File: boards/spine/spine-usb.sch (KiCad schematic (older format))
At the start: 34 parts, among them P1 USB_B, U1 93C56, U2 FT2232H, Y1 12 MHz

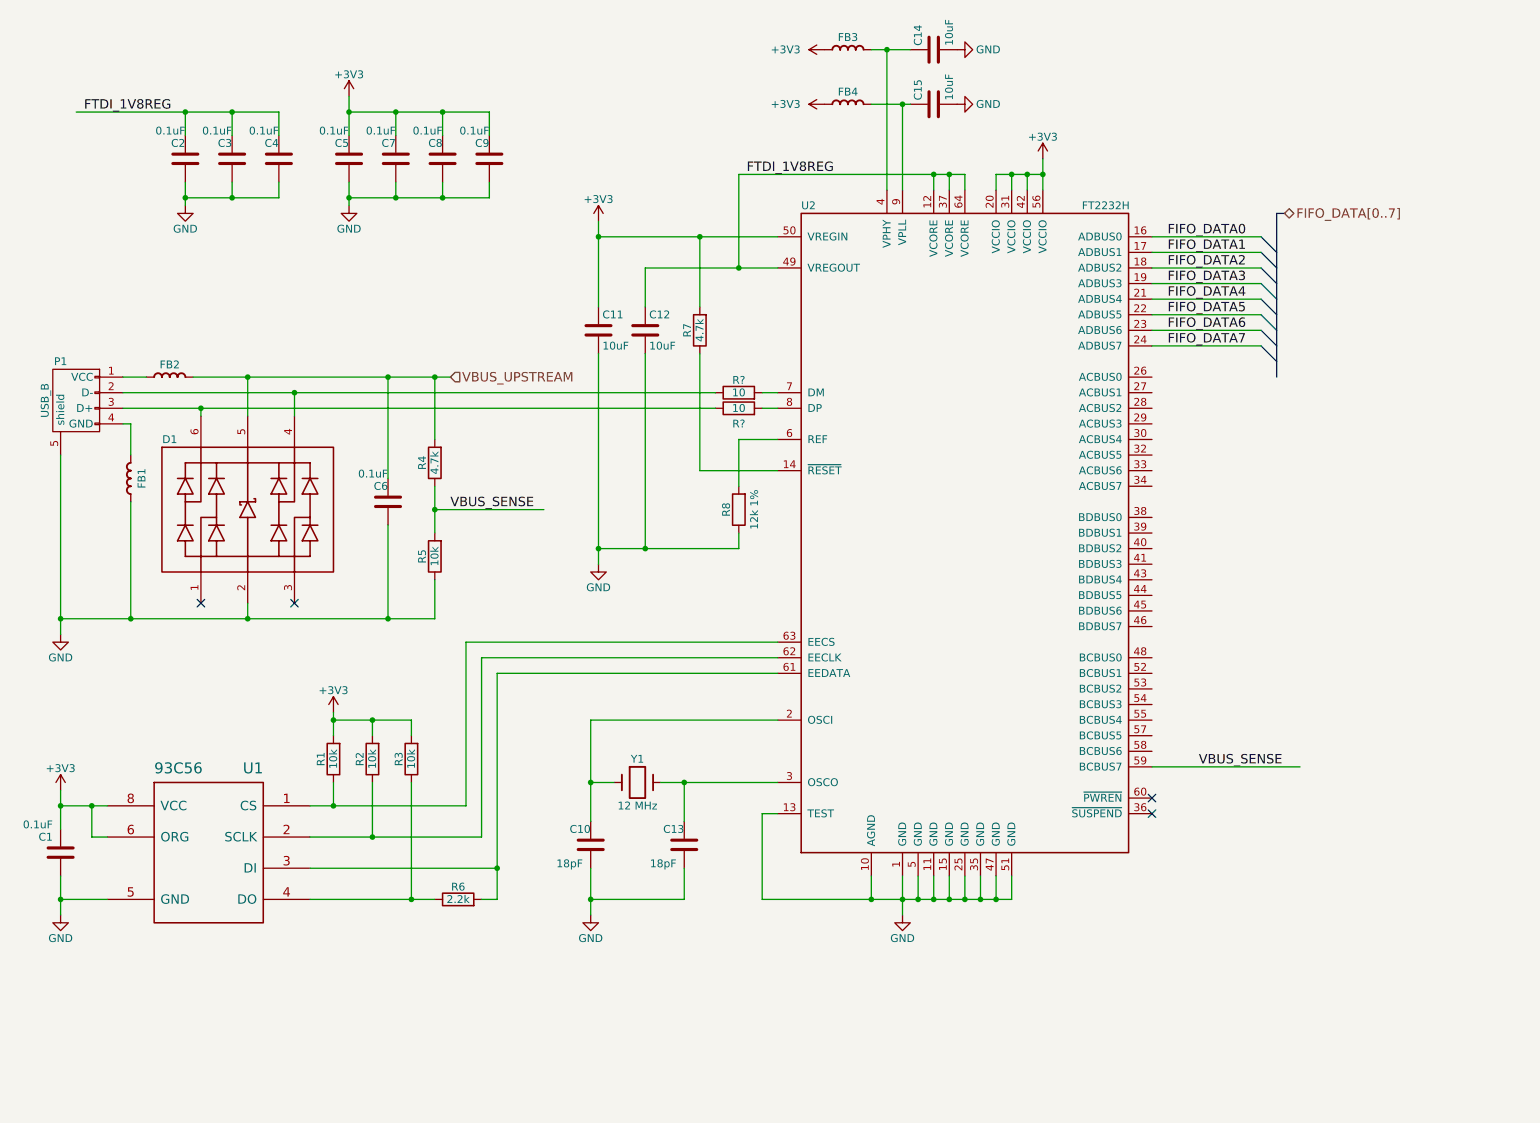
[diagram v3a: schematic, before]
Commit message: More schematic work: module ports and USB
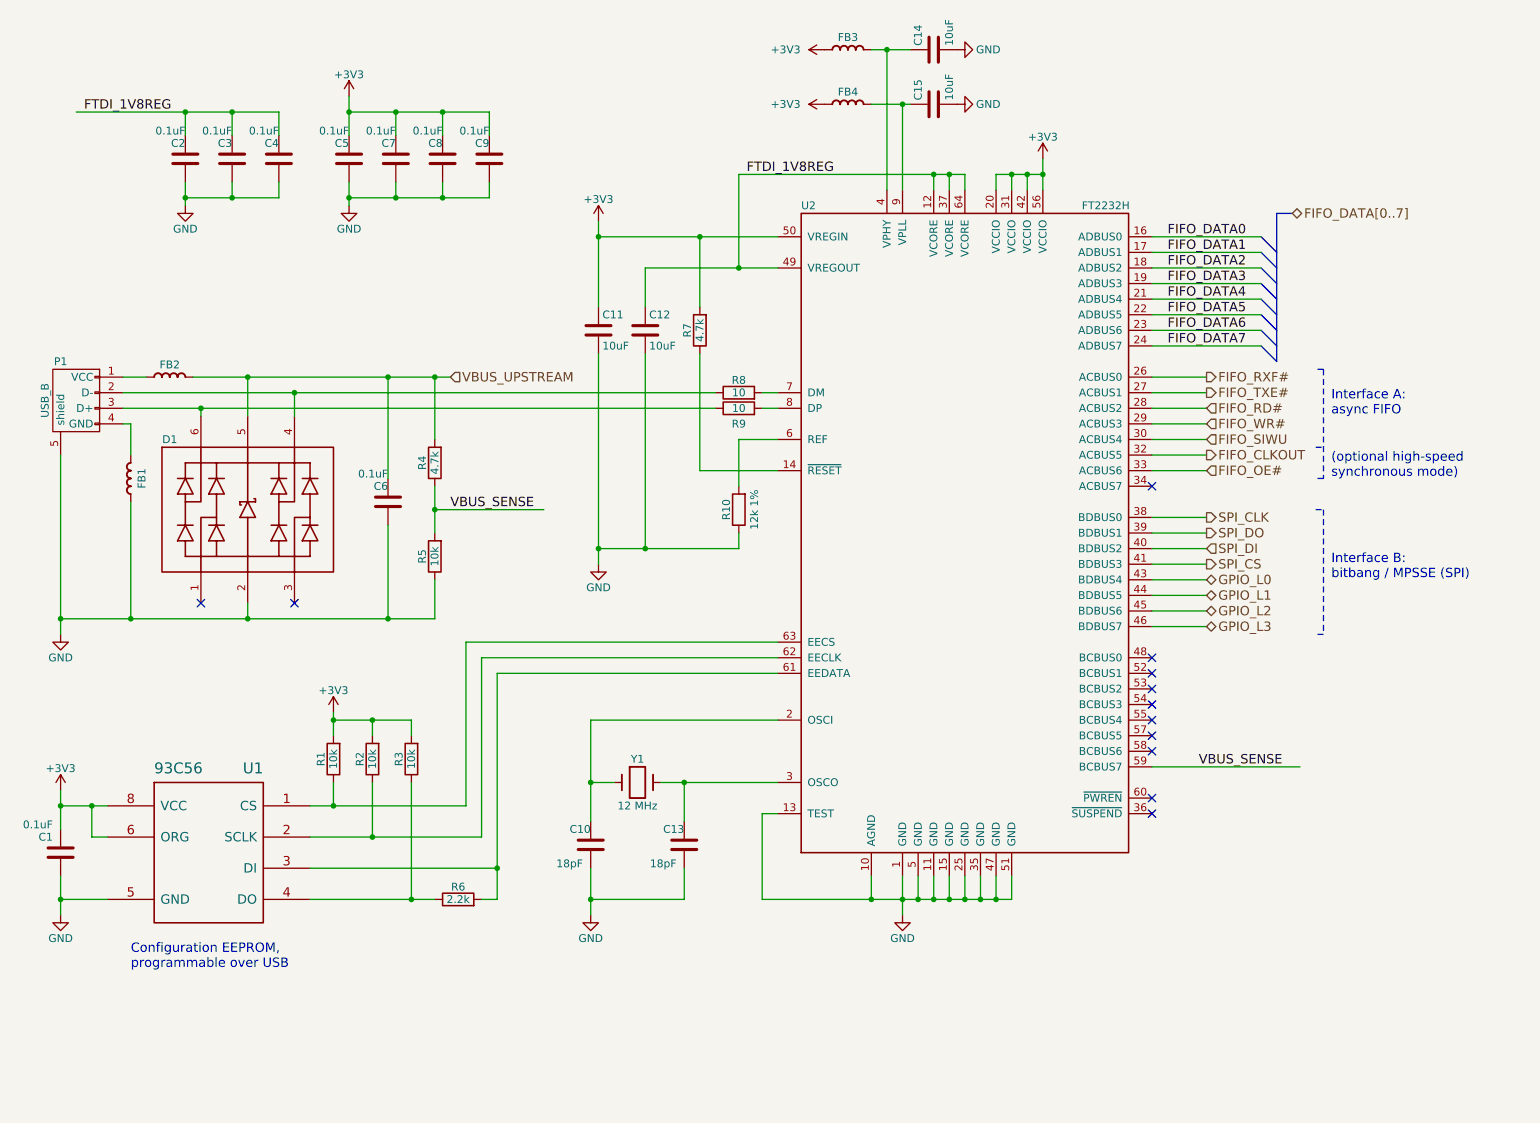
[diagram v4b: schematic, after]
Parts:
- gave numbers to parts that had none: 2
- renumbered R8 to R10
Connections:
- net labels added: FIFO_CLKOUT, FIFO_OE#, FIFO_RD#, FIFO_RXF#, FIFO_SIWU, FIFO_TXE#, FIFO_WR#, GPIO_L0, GPIO_L1, GPIO_L2, GPIO_L3, SPI_CLK, SPI_CS, SPI_DI, SPI_DO
- wire segments 119 -> 134
- no-connect marks 4 -> 12
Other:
- note added: "(optional high-speed\nsynchronous mode)"
- note added: "Configuration EEPROM,\nprogrammable over USB"
- note added: "Interface A:\nasync FIFO"
- note added: "Interface B:\nbitbang / MPSSE (SPI)"
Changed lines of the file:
@@
 $Descr USLetter 11000 8500
 encoding utf-8
-Sheet 2 4
+Sheet 2 5
 Title ""
 Date ""
@@
 	0    -1   1    0
 $EndComp
-Text HLabel 8900 1900 2    60   BiDi ~ 0
+Text HLabel 8950 1900 2    60   BiDi ~ 0
 FIFO_DATA[0..7]
 Entry Bus Bus
@@
 VBUS_SENSE
 $Comp
-L R R8
+L R R10
 U 1 1 563F3115
 P 5400 3800
-F 0 "R8" V 5480 3800 50  0000 C CNN
+F 0 "R10" V 5480 3800 50  0000 C CNN
 F 1 "12k 1%" V 5300 3800 50  0000 C CNN
 F 2 "" V 5330 3800 30  0000 C CNN
@@
 $EndComp
 $Comp
-L GND #PWR1
+L GND #PWR01
 U 1 1 563F3C00
 P 1050 4600
-F 0 "#PWR1" H 1050 4350 50  0001 C CNN
+F 0 "#PWR01" H 1050 4350 50  0001 C CNN
 F 1 "GND" H 1050 4450 50  0000 C CNN
 F 2 "" H 1050 4600 60  0000 C CNN
@@
 $EndComp
 $Comp
-L +3V3 #PWR9
+L +3V3 #PWR02
 U 1 1 563F5B33
 P 4500 1950
-F 0 "#PWR9" H 4500 1800 50  0001 C CNN
+F 0 "#PWR02" H 4500 1800 50  0001 C CNN
 F 1 "+3V3" H 4500 2090 50  0000 C CNN
 F 2 "" H 4500 1950 60  0000 C CNN
@@
 $EndComp
 $Comp
-L GND #PWR10
+L GND #PWR03
 U 1 1 56407FC9
 P 4500 4150
-F 0 "#PWR10" H 4500 3900 50  0001 C CNN
+F 0 "#PWR03" H 4500 3900 50  0001 C CNN
 F 1 "GND" H 4500 4000 50  0000 C CNN
 F 2 "" H 4500 4150 60  0000 C CNN
@@
 $EndComp
 $Comp
-L +3V3 #PWR12
+L +3V3 #PWR04
 U 1 1 56409317
 P 5950 1200
-F 0 "#PWR12" H 5950 1050 50  0001 C CNN
+F 0 "#PWR04" H 5950 1050 50  0001 C CNN
 F 1 "+3V3" V 5950 1450 50  0000 C CNN
 F 2 "" H 5950 1200 60  0000 C CNN
@@
 $EndComp
 $Comp
-L GND #PWR15
+L GND #PWR05
 U 1 1 56409352
 P 6800 1200
-F 0 "#PWR15" H 6800 950 50  0001 C CNN
+F 0 "#PWR05" H 6800 950 50  0001 C CNN
 F 1 "GND" V 6800 1000 50  0000 C CNN
 F 2 "" H 6800 1200 60  0000 C CNN
@@
 $EndComp
 $Comp
-L +3V3 #PWR11
+L +3V3 #PWR06
 U 1 1 564099D6
 P 5950 850
-F 0 "#PWR11" H 5950 700 50  0001 C CNN
+F 0 "#PWR06" H 5950 700 50  0001 C CNN
 F 1 "+3V3" V 5950 1100 50  0000 C CNN
 F 2 "" H 5950 850 60  0000 C CNN
@@
 $EndComp
 $Comp
-L GND #PWR14
+L GND #PWR07
 U 1 1 564099DC
 P 6800 850
-F 0 "#PWR14" H 6800 600 50  0001 C CNN
+F 0 "#PWR07" H 6800 600 50  0001 C CNN
 F 1 "GND" V 6800 650 50  0000 C CNN
 F 2 "" H 6800 850 60  0000 C CNN
@@
 $EndComp
 $Comp
-L +3V3 #PWR16
+L +3V3 #PWR08
 U 1 1 56409B2C
 P 7350 1550
-F 0 "#PWR16" H 7350 1400 50  0001 C CNN
+F 0 "#PWR08" H 7350 1400 50  0001 C CNN
 F 1 "+3V3" H 7350 1690 50  0000 C CNN
 F 2 "" H 7350 1550 60  0000 C CNN
@@
 $EndComp
 $Comp
-L +3V3 #PWR2
+L +3V3 #PWR09
 U 1 1 5640C498
 P 1050 5600
-F 0 "#PWR2" H 1050 5450 50  0001 C CNN
+F 0 "#PWR09" H 1050 5450 50  0001 C CNN
 F 1 "+3V3" H 1050 5740 50  0000 C CNN
 F 2 "" H 1050 5600 60  0000 C CNN
@@
 $EndComp
 $Comp
-L GND #PWR3
+L GND #PWR010
 U 1 1 5640C700
 P 1050 6400
-F 0 "#PWR3" H 1050 6150 50  0001 C CNN
+F 0 "#PWR010" H 1050 6150 50  0001 C CNN
 F 1 "GND" H 1050 6250 50  0000 C CNN
 F 2 "" H 1050 6400 60  0000 C CNN
@@
 $EndComp
 $Comp
-L +3V3 #PWR5
+L +3V3 #PWR011
 U 1 1 5640CB0D
 P 2800 5100
-F 0 "#PWR5" H 2800 4950 50  0001 C CNN
+F 0 "#PWR011" H 2800 4950 50  0001 C CNN
 F 1 "+3V3" H 2800 5240 50  0000 C CNN
 F 2 "" H 2800 5100 60  0000 C CNN
@@
 $EndComp
 $Comp
-L GND #PWR4
+L GND #PWR012
 U 1 1 5640EC58
 P 1850 1850
-F 0 "#PWR4" H 1850 1600 50  0001 C CNN
+F 0 "#PWR012" H 1850 1600 50  0001 C CNN
 F 1 "GND" H 1850 1700 50  0000 C CNN
 F 2 "" H 1850 1850 60  0000 C CNN
@@
 $EndComp
 $Comp
-L GND #PWR7
+L GND #PWR013
 U 1 1 5640ECEA
 P 2900 1850
-F 0 "#PWR7" H 2900 1600 50  0001 C CNN
+F 0 "#PWR013" H 2900 1600 50  0001 C CNN
 F 1 "GND" H 2900 1700 50  0000 C CNN
 F 2 "" H 2900 1850 60  0000 C CNN
@@
 FTDI_1V8REG
 $Comp
-L +3V3 #PWR6
+L +3V3 #PWR014
 U 1 1 5640F443
 P 2900 1150
-F 0 "#PWR6" H 2900 1000 50  0001 C CNN
+F 0 "#PWR014" H 2900 1000 50  0001 C CNN
 F 1 "+3V3" H 2900 1290 50  0000 C CNN
 F 2 "" H 2900 1150 60  0000 C CNN
@@
 $EndComp
 $Comp
-L GND #PWR8
+L GND #PWR015
 U 1 1 56411C34
 P 4450 6400
-F 0 "#PWR8" H 4450 6150 50  0001 C CNN
+F 0 "#PWR015" H 4450 6150 50  0001 C CNN
 F 1 "GND" H 4450 6250 50  0000 C CNN
 F 2 "" H 4450 6400 60  0000 C CNN
@@
 $EndComp
 $Comp
-L GND #PWR13
+L GND #PWR016
 U 1 1 56412014
 P 6450 6400
-F 0 "#PWR13" H 6450 6150 50  0001 C CNN
+F 0 "#PWR016" H 6450 6150 50  0001 C CNN
 F 1 "GND" H 6450 6250 50  0000 C CNN
 F 2 "" H 6450 6400 60  0000 C CNN
@@
 	8050 2050 8750 2050
 Wire Bus Line
-	8850 1900 8850 2950
+	8850 1900 8850 2850
 Wire Bus Line
-	8850 1900 8900 1900
+	8850 1900 8950 1900
 Wire Wire Line
 	1450 2950 1600 2950
@@
 Connection ~ 4450 6300
 $Comp
-L R R?
+L R R8
 U 1 1 56413618
 P 5400 3050
-F 0 "R?" V 5480 3050 50  0000 C CNN
+F 0 "R8" V 5480 3050 50  0000 C CNN
 F 1 "10" V 5400 3050 50  0000 C CNN
 F 2 "" V 5330 3050 30  0000 C CNN
@@
 $EndComp
 $Comp
-L R R?
+L R R9
 U 1 1 56413B05
 P 5400 3150
-F 0 "R?" V 5300 3150 50  0000 C CNN
+F 0 "R9" V 5300 3150 50  0000 C CNN
 F 1 "10" V 5400 3150 50  0000 C CNN
 F 2 "" V 5330 3150 30  0000 C CNN
@@
 Wire Wire Line
 	5650 3150 5550 3150
+Text HLabel 8400 2950 2    60   Output ~ 0
+FIFO_RXF#
+Text HLabel 8400 3050 2    60   Output ~ 0
+FIFO_TXE#
+Text HLabel 8400 3150 2    60   Input ~ 0
+FIFO_RD#
+Text HLabel 8400 3250 2    60   Input ~ 0
+FIFO_WR#
+Text HLabel 8400 3350 2    60   Input ~ 0
+FIFO_SIWU
+Text HLabel 8400 3450 2    60   Output ~ 0
+FIFO_CLKOUT
+Text HLabel 8400 3550 2    60   Input ~ 0
+FIFO_OE#
+Wire Notes Line
+	9100 3400 9150 3400
+Wire Notes Line
+	9150 2900 9150 3600
+Wire Notes Line
+	9150 3600 9100 3600
+Text Notes 9200 3600 0    60   ~ 0
+(optional high-speed\nsynchronous mode)
+Text HLabel 8400 3850 2    60   Output ~ 0
+SPI_CLK
+Text HLabel 8400 3950 2    60   Output ~ 0
+SPI_DO
+Text HLabel 8400 4050 2    60   Input ~ 0
+SPI_DI
+Text HLabel 8400 4150 2    60   Output ~ 0
+SPI_CS
+Text HLabel 8400 4250 2    60   BiDi ~ 0
+GPIO_L0
+Text HLabel 8400 4450 2    60   BiDi ~ 0
+GPIO_L2
+Text HLabel 8400 4350 2    60   BiDi ~ 0
+GPIO_L1
+Text HLabel 8400 4550 2    60   BiDi ~ 0
+GPIO_L3
+NoConn ~ 8050 3650
+Wire Wire Line
+	8050 2950 8400 2950
+Wire Wire Line
+	8050 3050 8400 3050
+Wire Wire Line
+	8400 3150 8050 3150
+Wire Wire Line
+	8050 3250 8400 3250
+Wire Wire Line
+	8400 3350 8050 3350
+Wire Wire Line
+	8050 3450 8400 3450
+Wire Wire Line
+	8400 3550 8050 3550
+Wire Wire Line
+	8050 3850 8400 3850
+Wire Wire Line
+	8400 3950 8050 3950
+Wire Notes Line
+	9150 2900 9100 2900
+Text Notes 9200 3200 0    60   ~ 0
+Interface A:\nasync FIFO
+Wire Notes Line
+	9100 3800 9150 3800
+Wire Notes Line
+	9150 3800 9150 4600
+Wire Notes Line
+	9150 4600 9100 4600
+Text Notes 9200 4250 0    60   ~ 0
+Interface B:\nbitbang / MPSSE (SPI)
+Wire Wire Line
+	8400 4050 8050 4050
+Wire Wire Line
+	8050 4150 8400 4150
+Wire Wire Line
+	8400 4250 8050 4250
+Wire Wire Line
+	8050 4350 8400 4350
+Wire Wire Line
+	8050 4450 8400 4450
+Wire Wire Line
+	8400 4550 8050 4550
+NoConn ~ 8050 4750
+NoConn ~ 8050 4850
+NoConn ~ 8050 4950
+NoConn ~ 8050 5050
+NoConn ~ 8050 5150
+NoConn ~ 8050 5250
+NoConn ~ 8050 5350
+Text Notes 1500 6750 0    60   ~ 0
+Configuration EEPROM,\nprogrammable over USB
 $EndSCHEMATC
